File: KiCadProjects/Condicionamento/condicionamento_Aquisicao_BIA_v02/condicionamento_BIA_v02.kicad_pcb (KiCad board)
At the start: 2 copper layers, 90 x 100 mm, 36 parts, among them J1 Vref, J10 nó3, J11 nó4, J12 Amp_E1, J13 Amp_E2, J15 AmpI1, J16 Amp_E2, J17 AmpI1, J2 tensoes, J3 sinais analogicos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

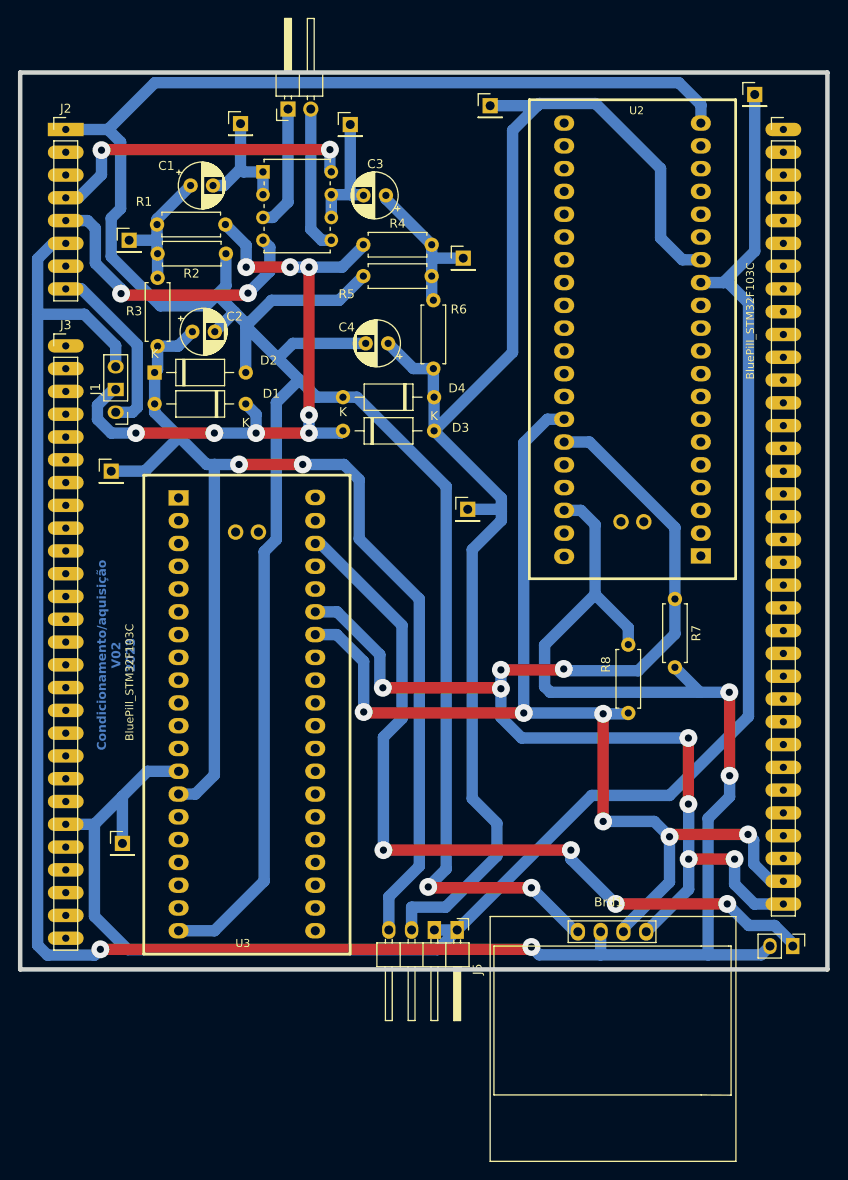
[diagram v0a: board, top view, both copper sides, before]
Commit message: Novos tamanhos pads
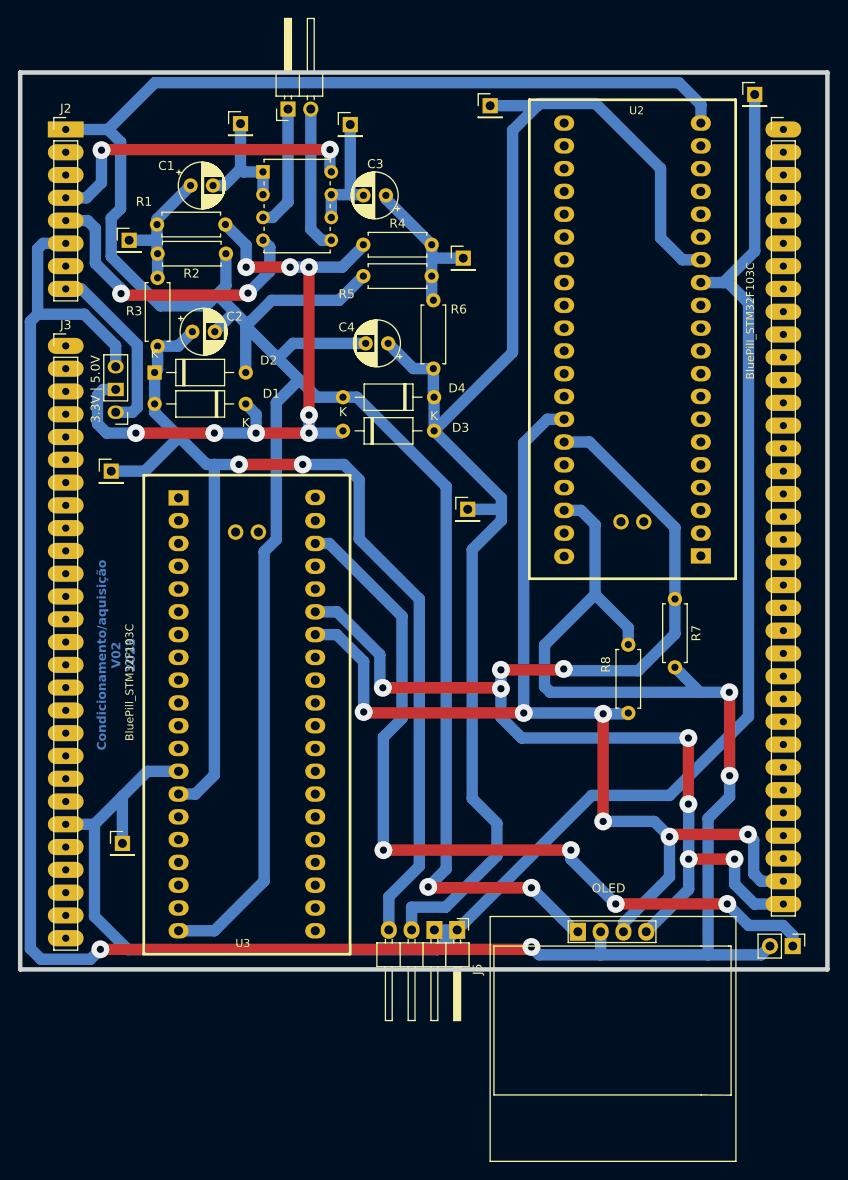
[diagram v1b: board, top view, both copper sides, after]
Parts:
- 3.3V | 5.0V: renamed from J1
- J5: value sinais_condicionados -> Amp_E1 | Amp_E2 | AmpI1 | AmpI1
- J6: value alimetacao_Master -> Vmaster
- renumbered Brd1 to OLED
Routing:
- net +5V: track 265.4 -> 267.8 mm
- net Net-(J6-Pin_1): track 90.2 -> 91.3 mm
- net Vref: track 73.9 -> 74.9 mm
- net SCL1: track 126.9 -> 127.6 mm
- net +9V: track 35.8 -> 36.3 mm

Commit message: Novos tamanhos pads
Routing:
- net -9V: track 33.7 -> 34.7 mm
- net Earth: track 313.2 -> 313.8 mm
